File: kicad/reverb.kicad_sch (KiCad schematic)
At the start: 22 parts, among them IC1 TL072CP

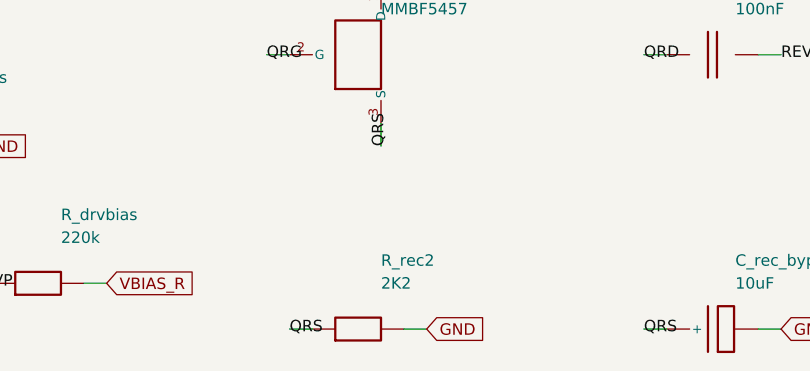
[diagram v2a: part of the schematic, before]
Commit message: Normalize BOM value strings; refresh stale top-level README
- gen_kicad NV(): normalize value strings for a tidy/consolidated BOM (2K2->2.2k,
  4K7->4.7k, drop the " film" descriptor that the footprint already conveys).
  Cosmetic only; ERC 0, demo DRC 0, SPICE exit 0, BOM regenerated.
- README rewritten to reflect the actual current state instead of the original
  reconstructed-docs snapshot: the generated + tool-verified KiCad/BOM/ngspice
  flow, the verified ~12 W power ceiling (not 18 W), the required mains fuse, the
  190x115 board + chassis-fit caveat, the active effects-chain/tone redesigns,
  and the provenance/honesty framing.

https://claude.ai/code/session_01PkrfUi9tvZfLvudJ7h23qD
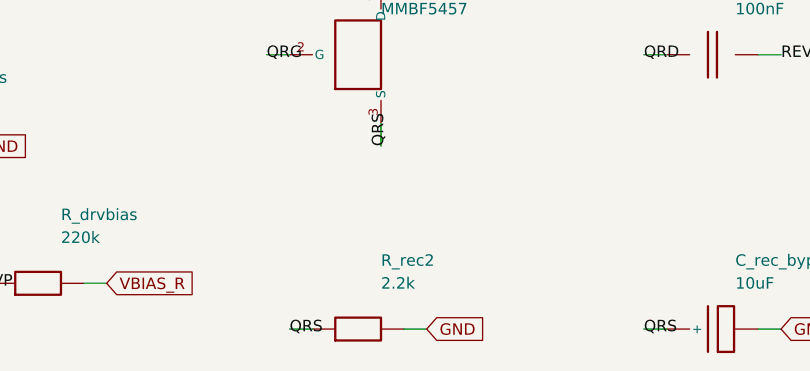
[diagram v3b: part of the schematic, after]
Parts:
- R_rec2: value 2K2 -> 2.2k
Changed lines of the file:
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@@
     (pin "8")
     (pin "4")
-    (instances (project "cambridge_reverb" (path "/516435f3-a06d-403b-8ebc-54e9b645518e" (reference "IC1") (unit 1))))
+    (instances (project "cambridge_reverb" (path "/205fc8d1-d038-4a7a-84cc-abb307413883" (reference "IC1") (unit 1))))
   )
   (wire (pts (xy 165.1 111.76) (xy 162.56 111.76)) (stroke (width 0) (type default)))
@@
     (pin "1")
     (pin "2")
-    (instances (project "cambridge_reverb" (path "/516435f3-a06d-403b-8ebc-54e9b645518e" (reference "C_drvin") (unit 1))))
+    (instances (project "cambridge_reverb" (path "/205fc8d1-d038-4a7a-84cc-abb307413883" (reference "C_drvin") (unit 1))))
   )
   (wire (pts (xy 101.6 201.93) (xy 99.06 201.93)) (stroke (width 0) (type default)))
@@
     (pin "1")
     (pin "2")
-    (instances (project "cambridge_reverb" (path "/516435f3-a06d-403b-8ebc-54e9b645518e" (reference "R_drvbias") (unit 1))))
+    (instances (project "cambridge_reverb" (path "/205fc8d1-d038-4a7a-84cc-abb307413883" (reference "R_drvbias") (unit 1))))
   )
   (wire (pts (xy 137.16000000000003 201.93) (xy 134.62 201.93)) (stroke (width 0) (type default)))
@@
     (pin "1")
     (pin "2")
-    (instances (project "cambridge_reverb" (path "/516435f3-a06d-403b-8ebc-54e9b645518e" (reference "R_drv1") (unit 1))))
+    (instances (project "cambridge_reverb" (path "/205fc8d1-d038-4a7a-84cc-abb307413883" (reference "R_drv1") (unit 1))))
   )
   (wire (pts (xy 212.09 91.44) (xy 209.55 91.44)) (stroke (width 0) (type default)))
@@
     (pin "1")
     (pin "2")
-    (instances (project "cambridge_reverb" (path "/516435f3-a06d-403b-8ebc-54e9b645518e" (reference "R_drv2") (unit 1))))
+    (instances (project "cambridge_reverb" (path "/205fc8d1-d038-4a7a-84cc-abb307413883" (reference "R_drv2") (unit 1))))
   )
   (wire (pts (xy 212.09 147.32) (xy 209.55 147.32)) (stroke (width 0) (type default)))
@@
     (pin "1")
     (pin "2")
-    (instances (project "cambridge_reverb" (path "/516435f3-a06d-403b-8ebc-54e9b645518e" (reference "C_rev1") (unit 1))))
+    (instances (project "cambridge_reverb" (path "/205fc8d1-d038-4a7a-84cc-abb307413883" (reference "C_rev1") (unit 1))))
   )
   (wire (pts (xy 222.25 116.84) (xy 219.71 116.84)) (stroke (width 0) (type default)))
@@
     (pin "1")
     (pin "2")
-    (instances (project "cambridge_reverb" (path "/516435f3-a06d-403b-8ebc-54e9b645518e" (reference "R_drv3") (unit 1))))
+    (instances (project "cambridge_reverb" (path "/205fc8d1-d038-4a7a-84cc-abb307413883" (reference "R_drv3") (unit 1))))
   )
   (wire (pts (xy 257.81 116.84) (xy 255.27 116.84)) (stroke (width 0) (type default)))
@@
     (pin "3")
     (pin "4")
-    (instances (project "cambridge_reverb" (path "/516435f3-a06d-403b-8ebc-54e9b645518e" (reference "REV1") (unit 1))))
+    (instances (project "cambridge_reverb" (path "/205fc8d1-d038-4a7a-84cc-abb307413883" (reference "REV1") (unit 1))))
   )
   (wire (pts (xy 293.37 121.92) (xy 290.83000000000004 121.92)) (stroke (width 0) (type default)))
@@
     (pin "1")
     (pin "2")
-    (instances (project "cambridge_reverb" (path "/516435f3-a06d-403b-8ebc-54e9b645518e" (reference "C_rev2") (unit 1))))
+    (instances (project "cambridge_reverb" (path "/205fc8d1-d038-4a7a-84cc-abb307413883" (reference "C_rev2") (unit 1))))
   )
   (wire (pts (xy 121.92 156.20999999999998) (xy 119.38 156.20999999999998)) (stroke (width 0) (type default)))
@@
     (pin "1")
     (pin "3")
-    (instances (project "cambridge_reverb" (path "/516435f3-a06d-403b-8ebc-54e9b645518e" (reference "Q_rec") (unit 1))))
+    (instances (project "cambridge_reverb" (path "/205fc8d1-d038-4a7a-84cc-abb307413883" (reference "Q_rec") (unit 1))))
   )
   (wire (pts (xy 170.18 176.52999999999997) (xy 167.64 176.52999999999997)) (stroke (width 0) (type default)))
@@
     (pin "1")
     (pin "2")
-    (instances (project "cambridge_reverb" (path "/516435f3-a06d-403b-8ebc-54e9b645518e" (reference "R_rec_bias") (unit 1))))
+    (instances (project "cambridge_reverb" (path "/205fc8d1-d038-4a7a-84cc-abb307413883" (reference "R_rec_bias") (unit 1))))
   )
   (wire (pts (xy 121.92 186.69) (xy 119.38 186.69)) (stroke (width 0) (type default)))
@@
     (pin "1")
     (pin "2")
-    (instances (project "cambridge_reverb" (path "/516435f3-a06d-403b-8ebc-54e9b645518e" (reference "R_rec1") (unit 1))))
+    (instances (project "cambridge_reverb" (path "/205fc8d1-d038-4a7a-84cc-abb307413883" (reference "R_rec1") (unit 1))))
   )
   (wire (pts (xy 172.72 152.39999999999998) (xy 170.18 152.39999999999998)) (stroke (width 0) (type default)))
@@
     (in_bom yes) (on_board yes) (dnp no)
     (property "Reference" "R_rec2" (at 180.34 199.39 0) (effects (font (size 1.27 1.27)) (justify left)))
-    (property "Value" "2K2" (at 180.34 201.92999999999998 0) (effects (font (size 1.27 1.27)) (justify left)))
+    (property "Value" "2.2k" (at 180.34 201.92999999999998 0) (effects (font (size 1.27 1.27)) (justify left)))
     (property "Footprint" "Resistor_THT:R_Axial_DIN0207_L6.3mm_D2.5mm_P5.08mm_Vertical" (at 177.8 207.01 0) (effects (font (size 1.27 1.27)) hide))
     (pin "1")
     (pin "2")
-    (instances (project "cambridge_reverb" (path "/516435f3-a06d-403b-8ebc-54e9b645518e" (reference "R_rec2") (unit 1))))
+    (instances (project "cambridge_reverb" (path "/205fc8d1-d038-4a7a-84cc-abb307413883" (reference "R_rec2") (unit 1))))
   )
   (wire (pts (xy 172.72 207.01) (xy 170.18 207.01)) (stroke (width 0) (type default)))
@@
     (pin "1")
     (pin "2")
-    (instances (project "cambridge_reverb" (path "/516435f3-a06d-403b-8ebc-54e9b645518e" (reference "C_rec_byp") (unit 1))))
+    (instances (project "cambridge_reverb" (path "/205fc8d1-d038-4a7a-84cc-abb307413883" (reference "C_rec_byp") (unit 1))))
   )
   (wire (pts (xy 212.09 207.01) (xy 209.55 207.01)) (stroke (width 0) (type default)))
@@
     (pin "1")
     (pin "2")
-    (instances (project "cambridge_reverb" (path "/516435f3-a06d-403b-8ebc-54e9b645518e" (reference "C_rev4") (unit 1))))
+    (instances (project "cambridge_reverb" (path "/205fc8d1-d038-4a7a-84cc-abb307413883" (reference "C_rev4") (unit 1))))
   )
   (wire (pts (xy 212.09 176.52999999999997) (xy 209.55 176.52999999999997)) (stroke (width 0) (type default)))
@@
     (pin "3")
     (pin "2")
-    (instances (project "cambridge_reverb" (path "/516435f3-a06d-403b-8ebc-54e9b645518e" (reference "POT_REV") (unit 1))))
+    (instances (project "cambridge_reverb" (path "/205fc8d1-d038-4a7a-84cc-abb307413883" (reference "POT_REV") (unit 1))))
   )
   (wire (pts (xy 261.62 186.69) (xy 259.08 186.69)) (stroke (width 0) (type default)))
@@
     (pin "1")
     (pin "2")
-    (instances (project "cambridge_reverb" (path "/516435f3-a06d-403b-8ebc-54e9b645518e" (reference "R_mixfb") (unit 1))))
+    (instances (project "cambridge_reverb" (path "/205fc8d1-d038-4a7a-84cc-abb307413883" (reference "R_mixfb") (unit 1))))
   )
   (wire (pts (xy 152.4 91.44) (xy 149.86 91.44)) (stroke (width 0) (type default)))
@@
     (pin "1")
     (pin "2")
-    (instances (project "cambridge_reverb" (path "/516435f3-a06d-403b-8ebc-54e9b645518e" (reference "C_drymix") (unit 1))))
+    (instances (project "cambridge_reverb" (path "/205fc8d1-d038-4a7a-84cc-abb307413883" (reference "C_drymix") (unit 1))))
   )
   (wire (pts (xy 82.55 76.19999999999999) (xy 80.01 76.19999999999999)) (stroke (width 0) (type default)))
@@
     (pin "1")
     (pin "2")
-    (instances (project "cambridge_reverb" (path "/516435f3-a06d-403b-8ebc-54e9b645518e" (reference "R_drymix") (unit 1))))
+    (instances (project "cambridge_reverb" (path "/205fc8d1-d038-4a7a-84cc-abb307413883" (reference "R_drymix") (unit 1))))
   )
   (wire (pts (xy 116.84 76.19999999999999) (xy 114.30000000000001 76.19999999999999)) (stroke (width 0) (type default)))
@@
     (pin "1")
     (pin "2")
-    (instances (project "cambridge_reverb" (path "/516435f3-a06d-403b-8ebc-54e9b645518e" (reference "C_wetmix") (unit 1))))
+    (instances (project "cambridge_reverb" (path "/205fc8d1-d038-4a7a-84cc-abb307413883" (reference "C_wetmix") (unit 1))))
   )
   (wire (pts (xy 292.1 186.69) (xy 289.56 186.69)) (stroke (width 0) (type default)))
@@
     (pin "1")
     (pin "2")
-    (instances (project "cambridge_reverb" (path "/516435f3-a06d-403b-8ebc-54e9b645518e" (reference "R_wetmix") (unit 1))))
+    (instances (project "cambridge_reverb" (path "/205fc8d1-d038-4a7a-84cc-abb307413883" (reference "R_wetmix") (unit 1))))
   )
   (wire (pts (xy 327.66 186.69) (xy 325.12 186.69)) (stroke (width 0) (type default)))
@@
     (pin "1")
     (pin "2")
-    (instances (project "cambridge_reverb" (path "/516435f3-a06d-403b-8ebc-54e9b645518e" (reference "R_fs_rev") (unit 1))))
+    (instances (project "cambridge_reverb" (path "/205fc8d1-d038-4a7a-84cc-abb307413883" (reference "R_fs_rev") (unit 1))))
   )
   (wire (pts (xy 92.71000000000001 207.01) (xy 90.17 207.01)) (stroke (width 0) (type default)))
